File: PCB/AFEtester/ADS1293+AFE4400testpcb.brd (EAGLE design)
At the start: 48.7 x 72.9 mm, 47 parts, among them IC1 ADS1293, J1 POWER_JACK, U2 TPS61093DSKT, Y1 4.096MHz

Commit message: afe4400 pcb stuff
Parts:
- added 3V3-POWER-TESTPOINT1, 3V3-POWER-TESTPOINT2: (no value), SparkFun-Connectors:1X02
- added C16: 1nF, SparkFun-Capacitors:0603
- added C17, C18, C19, C20, C22, C23, C24: 10uF, SparkFun-Retired:EIA3216
- added C21, C27: 10nF, SparkFun-Capacitors:0603
- added C25, C29, C30: 0.1uF, SparkFun-Capacitors:0603
- added C26: 1.0uF, SparkFun-Capacitors:0805
- added C28, C31: 2.2uF, SparkFun-Capacitors:0805
- added C32, C33: 18pF, SparkFun-Capacitors:0603
- added D1: GREEN, SparkFun-LED:LED-1206
- added D2, D3: BAV99S, nxp_60:SOT363
- added FRAME2: FRAME-LEDGER, SparkFun-Aesthetics:CREATIVE_COMMONS
- added IC2: LP3878MR-ADJ_NOPB, LP3878MR-ADJ_NOPB:SOIC127P602X168-9N
- added J3: (no value), SparkFun-Connectors:DB9
- added J4: (no value), SparkFun-Connectors:1X08
- added J5: (no value), SparkFun-Connectors:1X04
- added L2, L3, L4: 3.3µH/±20%/450mA, SparkFun-Coils:0805
- added R18, R29: 1k, SparkFun-Resistors:0603
- added R19: 4.7k, SparkFun-Resistors:0603
- added R20, R21, R24, R25, R26, R27, R28, R30, R31, R32, R33, R34, R35: 0, SparkFun-Resistors:0603
- added R22: 75k, SparkFun-Resistors:0603
- added R23: 47k, SparkFun-Resistors:0603
- added R36: 10, SparkFun-Resistors:0603
- added R37: 10k, SparkFun-Resistors:0603
- added R38, R39, R40, R41, R42, R43: 130, SparkFun-Resistors:0603
- added S2: MOMENTARY-SWITCH-SPST-PTH-6.0MM, SparkFun-Switches:TACTILE_SWITCH_PTH_6.0MM
- added U3: AFE4400_RHA_40, AFE4400:RHA40_4P15X4P15
- added Y2: 8MHz, SparkFun-Clocks:CRYSTAL-SMD-5X3.2-4PAD
- C13: device SparkFun-Capacitors:0805 -> SparkFun-Retired:EIA3216
- C14, C15: value 0.1uF -> 10nF
- L1: value LPS3010-102MRC -> 3.3µH/±20%/450mA; device LPS3010-102MRC:LPS3010102MRC -> SparkFun-Coils:0805
- R17: value 0 -> 2.55k
- U2: value TPS61093DSKT -> TPS7A4901DGNR; device Texas Instruments_By_element14_Batch_1:SON50P250X250X80-11N -> Texas Instruments_By_element14_Batch_1:SOP65P490X110-9N
- moved L1 106.1 mm to (76.7, 14.4)
- moved C14 92.4 mm to (64.9, 22.9), turned to 270 degrees
- moved R17 81.2 mm to (62.5, 11.0)
- moved C13 79.4 mm to (52.7, 19.5), turned to 180 degrees
- moved U2 77.2 mm to (58.3, 24.1)
- moved C15 76.0 mm to (48.4, 15.6), turned to 180 degrees
- moved R16 74.1 mm to (56.8, 8.97)
- moved S1 50.4 mm to (46.3, 92.0)
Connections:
- removed net C: COMM-CONN.6, IC1.17
- removed net VCC: C13.1, R16.1
- new net ADC_RDY: J4.5, U3.28
- new net AFE_PDN: J4.8, U3.20
- new net CLKOUT_AFE: J4.2, R36.2
- new net DIAG_END: J4.7, U3.21
- new net LED_ALM: J4.6, U3.22
- new net LED_DRV_SUP: C26.1, D3.2, D3.5, J5.1, R20.2, U3.17, U3.18
- new net N$21: 3V3-POWER-TESTPOINT1.2, C16.1, IC2.5, R17.2
- new net N$22: C14.1, U2.6
- new net N$23: C19.A, L1.2, R20.1
- new net N$24: C20.A, L2.2, R21.1
- new net N$25: C13.A, R26.1, U2.5, U2.8
- new net N$26: 3V3-POWER-TESTPOINT2.2, C21.1, R22.2, U2.1
- new net N$27: C21.2, R22.1, R23.2, U2.2
- new net N$28: C23.A, L3.2, R27.1
- new net N$29: C17.A, IC2.4, IC2.8, R25.1
- new net N$30: C24.A, L4.2, R28.1
- new net N$31: C28.2, U3.7
- new net N$32: C31.1, U3.9
- new net N$33: R32.2, U3.14
- new net N$34: R29.2, U3.4
- new net N$36: R31.2, U3.1
- new net N$37: R30.2, U3.2
- new net N$38: D2.3, J3.5, R31.1
- new net N$39: D2.6, J3.9, R30.1
- new net N$40: R33.2, U3.15
- new net N$41: D3.6, J3.3, R32.1
- new net N$42: D3.3, J3.2, R33.1
- new net N$43: C32.2, R34.2, Y2.1
- new net N$44: C33.1, R35.1, Y2.3
- new net N$45: R36.1, U3.30
- new net N$46: R37.2, S2.3, U3.29
- new net N$48: R35.2, U3.37
- new net N$49: R38.1, U3.35
- new net N$50: R42.1, U3.5
- new net N$52: R41.1, U3.6
- new net N$53: R40.1, U3.10
- new net N$54: R39.1, U3.34
- new net N$55: R38.2
- new net N$56: R39.2
- new net N$57: R40.2
- new net N$58: R41.2
- new net N$59: R42.2
- new net PD_ALM: J4.4, U3.23
- new net RX_ANA_SUP: C30.1, D2.2, D2.5, J5.4, R28.2, U3.33, U3.39
- new net RX_DIG_SUP: C29.1, J5.3, R27.2, R37.1, U3.31
- new net RX_SUP: 3V3-POWER-TESTPOINT2.1, C22.A, L3.1, L4.1
- new net SCLK: COMM-CONN.6, IC1.17, U3.24
- new net STE: J4.1, U3.27
- new net TX_CTRL_SUP: C25.1, J5.2, R21.2, U3.11
- new net VCM_SHIELD: C27.1, R29.1
- new net XIN_MSP: J4.3, R34.1, U3.38
- net +5V: now also D1.A, R25.2, R26.2
- net GND: now also C13.C, C14.2, C15.2, C17.C, C18.C, C19.C, C20.C, C22.C, C23.C, C24.C, C25.2, C26.2, C27.2, C28.1, C29.2, C30.2, C31.2, C32.1, C33.2, D2.1, D2.4, D3.1, D3.4, IC2.3, IC2.7, IC2.9, J3.7, R16.1, R16.2, R18.1, R19.1, R23.1, R24.1, R24.2, R43.1, S2.1, U2.4, U2.9, U3.12, U3.13, U3.16, U3.19, U3.3, U3.32, U3.36, U3.40, U3.41, U3.8; no longer C13.2, U2.1
- net MISO: now also U3.25
- net MOSI: now also U3.26
- net N$18: now also 3V3-POWER-TESTPOINT1.1, C18.A, L1.1, L2.1; no longer R17.2, U2.5
- net N$19: now also C16.2, IC2.6, R18.2; no longer R16.2, U2.2
- net N$20: now also C15.1, IC2.1; no longer C15.2, U2.3
- net N$4: now also D1.C, R19.2; no longer C15.1, U2.4
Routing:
- net GND: track 225.3 -> 414.5 mm, vias 8 -> 9
- net VCM_SHIELD: track 0.00 -> 47.1 mm, vias 0 -> 2
- net N$25: track 0.00 -> 31.4 mm, vias 0 -> 2
- net N$29: track 0.00 -> 28.6 mm
- net N$39: track 0.00 -> 26.4 mm, vias 0 -> 1
- net N$40: track 0.00 -> 20.8 mm
- net SCLK: track 0.00 -> 20.4 mm
- net C: track 20.4 -> 0.00 mm
- net N$33: track 0.00 -> 20.0 mm
- net RX_ANA_SUP: track 0.00 -> 18.4 mm, vias 0 -> 1
- net +5V: track 81.0 -> 99.3 mm
- net N$42: track 0.00 -> 17.9 mm, vias 0 -> 1
- net N$41: track 0.00 -> 17.3 mm, vias 0 -> 1
- net N$26: track 0.00 -> 16.3 mm, vias 0 -> 1
- net RSTBCON: track 52.7 -> 38.4 mm
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- removed copper zone on layer 1, net GND
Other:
- board size 48.7 x 72.9 mm -> 117 x 96.9 mm
- board text removed: "ADS1293-TEST-PCB-Rev. 01"
- board text removed: "JINGJIE LI, XJTU-BME"

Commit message: almost complete AFE PCB
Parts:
- removed FRAME2: FRAME-LEDGER, SparkFun-Aesthetics:CREATIVE_COMMONS
- J5: device SparkFun-Connectors:1X04 -> SparkFun-Connectors:1X05
- moved J4 59.0 mm to (42.1, 89.0), turned to 270 degrees
- moved R42 56.8 mm to (21.4, 79.2), turned to 180 degrees
- moved R43 56.8 mm to (21.3, 77.4), turned to 180 degrees
- moved R41 53.3 mm to (24.9, 79.2), turned to 180 degrees
- moved R40 51.9 mm to (27.4, 73.7), turned to 270 degrees
- moved J5 51.8 mm to (54.4, 32.0), turned to 90 degrees
- moved R39 43.1 mm to (35.1, 86.1)
- moved R38 42.3 mm to (35.9, 88.0)
- moved S2 15.2 mm to (41.8, 95.2)
- moved C28 11.2 mm to (24.9, 77.4)
- moved C26 8.66 mm to (33.1, 75.0), turned to 270 degrees
- moved S1 8.34 mm to (54.0, 95.3)
- moved R37 6.26 mm to (38.8, 81.8)
- moved C31 4.49 mm to (24.9, 75.2), turned to 180 degrees
- moved C25 3.84 mm to (29.6, 74.9), turned to 270 degrees
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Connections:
- net GND: now also J5.5; no longer R43.1
- net LED_DRV_SUP: now also J5.3; no longer J5.1
- net N$31: now also R43.1
- net RX_ANA_SUP: now also J5.1; no longer J5.4
- net RX_DIG_SUP: now also J5.2; no longer J5.3
- net TX_CTRL_SUP: now also J5.4; no longer J5.2
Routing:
- net GND: track 414.5 -> 763.2 mm, vias 9 -> 17
- net LED_DRV_SUP: track 11.1 -> 145.7 mm, vias 0 -> 1
- net RX_ANA_SUP: track 18.4 -> 150.3 mm
- net RX_DIG_SUP: track 7.25 -> 131.8 mm, vias 0 -> 2
- net TX_CTRL_SUP: track 0.00 -> 113.5 mm, vias 0 -> 2
- net MOSI: track 21.6 -> 55.1 mm, vias 0 -> 1
- net SCLK: track 20.4 -> 53.0 mm, vias 0 -> 1
- net MISO: track 17.5 -> 47.0 mm, vias 0 -> 1
- net RSTBCON: track 38.4 -> 66.6 mm, vias 1 -> 3
- net STE: track 0.00 -> 22.3 mm
- net N$46: track 9.42 -> 25.5 mm, vias 0 -> 1
- net XIN_MSP: track 5.28 -> 21.1 mm, vias 0 -> 1
- net LED_ALM: track 0.00 -> 12.4 mm
- net AFE_PDN: track 0.00 -> 12.2 mm
- net DIAG_END: track 0.00 -> 11.2 mm
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- added copper zone on layer 1, net GND
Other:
- board size 117 x 96.9 mm -> 117.4 x 101.5 mm

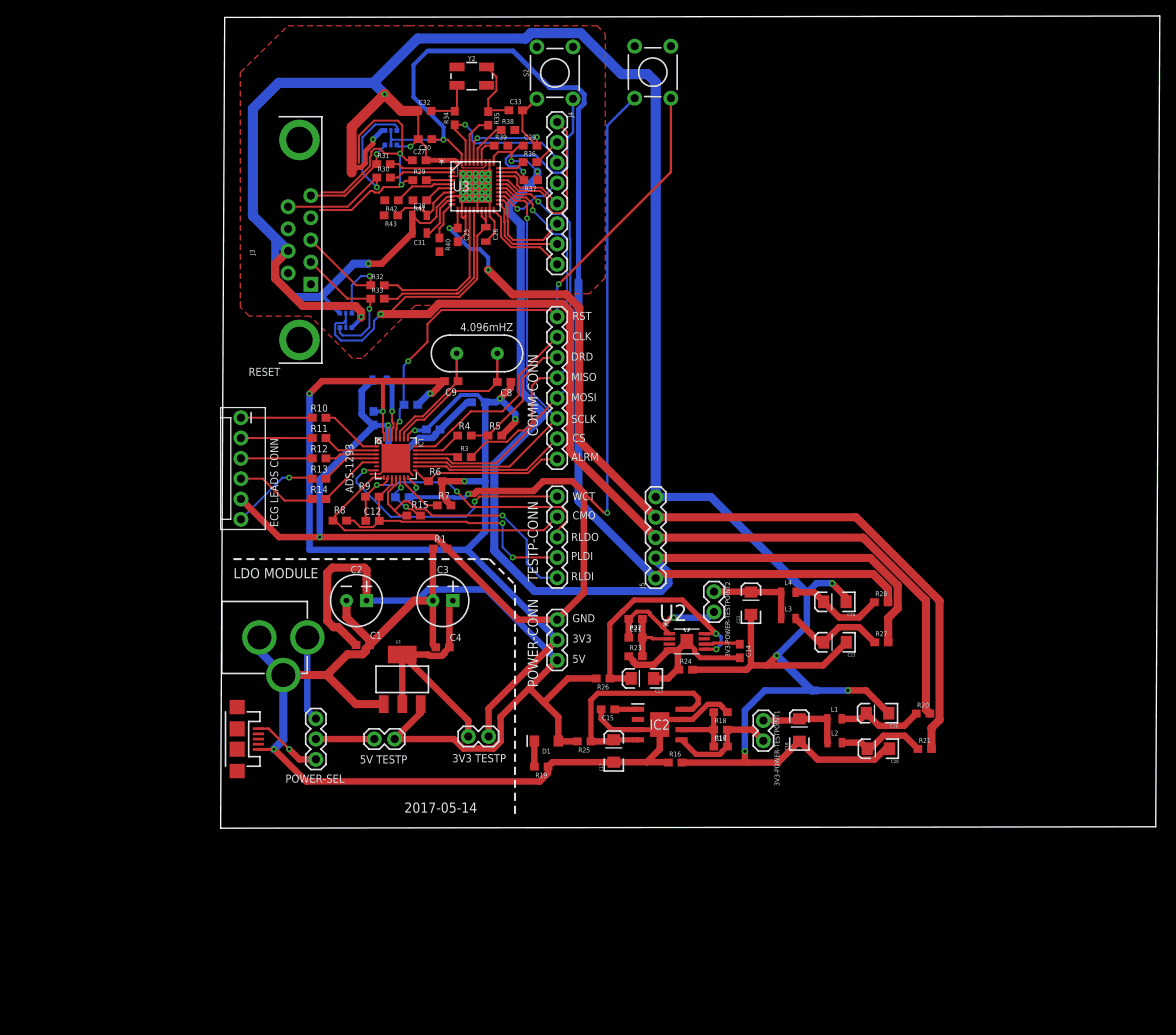
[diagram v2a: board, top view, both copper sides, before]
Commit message: Finishing ADS&AFE joint test pcb
exporting gerber
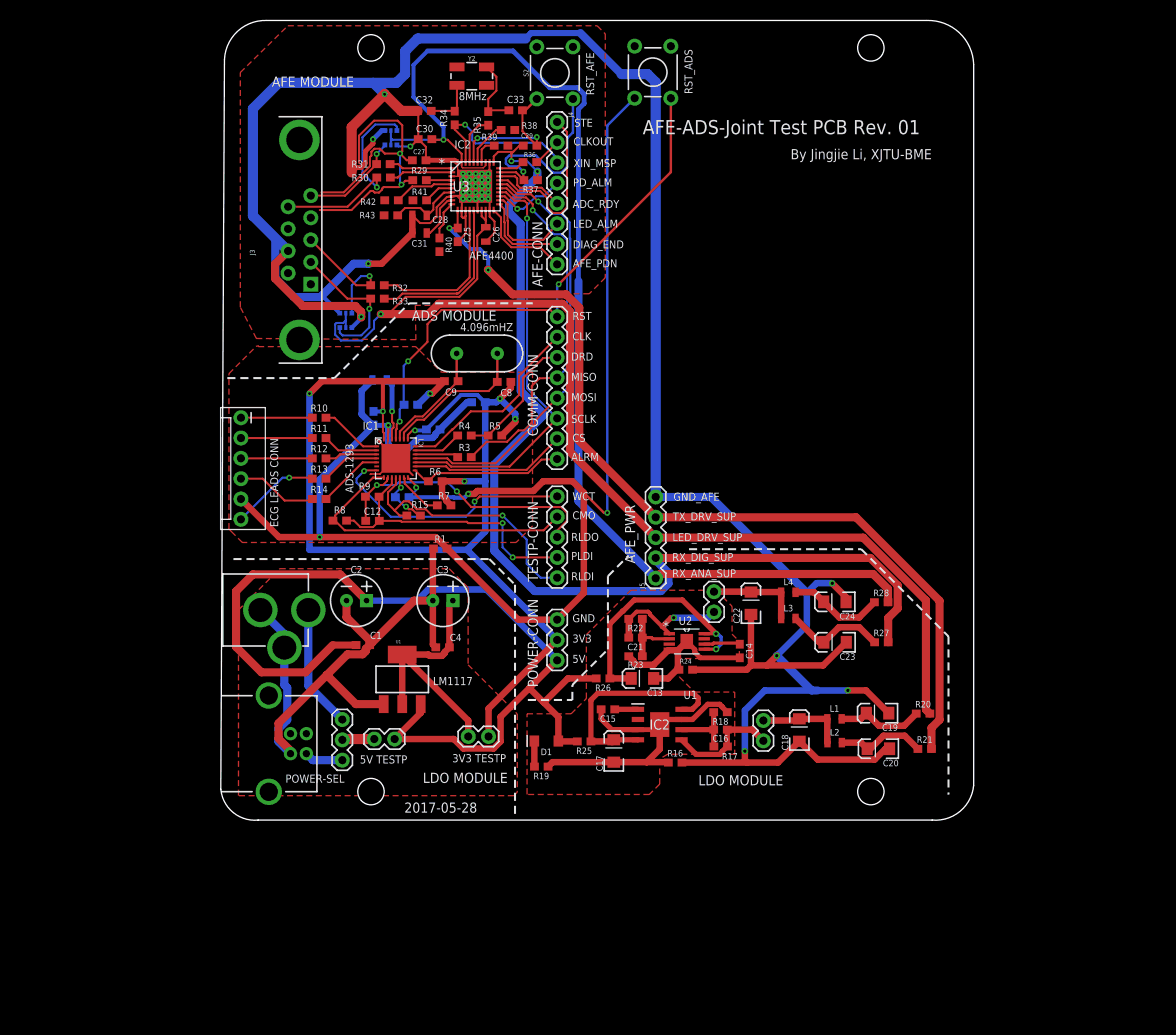
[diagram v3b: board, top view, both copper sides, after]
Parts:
- added U$1, U$2, U$3, U$4: (no value), SparkFun-Hardware:STAND-OFF
- J2: value (none) -> USB_B_PTH; device SparkFun-Connectors:USB-MICROB -> SparkFun-Connectors:USB-B-PTH
- moved J1 3.43 mm to (-2.73, 28.0)
- moved POWER-JUMPER 3.30 mm to (15.2, 14.3)
- moved J2 2.74 mm to (4.74, 11.3), turned to 0 degrees
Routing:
- net GND: track 763.2 -> 737.9 mm, vias 17 -> 16
- net +5V: track 99.3 -> 122.5 mm
- net N$3: track 10.6 -> 15.4 mm
- net N$2: track 8.78 -> 4.83 mm, vias 1 -> 0
- net N$16: track 7.30 -> 4.04 mm
- net N$64: track 0.00 -> 0.81 mm
- net N$63: track 0.00 -> 0.76 mm
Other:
- board size 117.4 x 101.5 mm -> 94.1 x 100 mm
- board text added: "2017-05-28"
- board text added: "8MHz"
- board text added: "ADC_RDY"
- board text added: "ADS MODULE"
- board text added: "AFE MODULE"
- board text added: "AFE-ADS-Joint Test PCB Rev. 01"
- board text added: "AFE-CONN"
- board text added: "AFE4400"
- board text added: "AFE_PDN"
- board text added: "AFE_PWR"
- board text added: "By Jingjie Li, XJTU-BME"
- board text added: "CLKOUT"
- board text added: "DIAG_END"
- board text added: "GND_AFE"
- board text added: "IC1"
- board text added: "IC2"
- board text added: "LED_ALM"
- board text added: "LED_DRV_SUP"
- board text added: "LM1117"
- board text added: "PD_ALM"
- board text added: "RST_ADS"
- board text added: "RST_AFE"
- board text added: "RX_ANA_SUP"
- board text added: "RX_DIG_SUP"
- board text added: "STE"
- board text added: "TX_DRV_SUP"
- board text added: "U1"
- board text added: "XIN_MSP"
- board text removed: "2017-05-14"
- board text removed: "RESET"
